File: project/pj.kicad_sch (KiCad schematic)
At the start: 2 parts, among them J1 RPi_GPIO

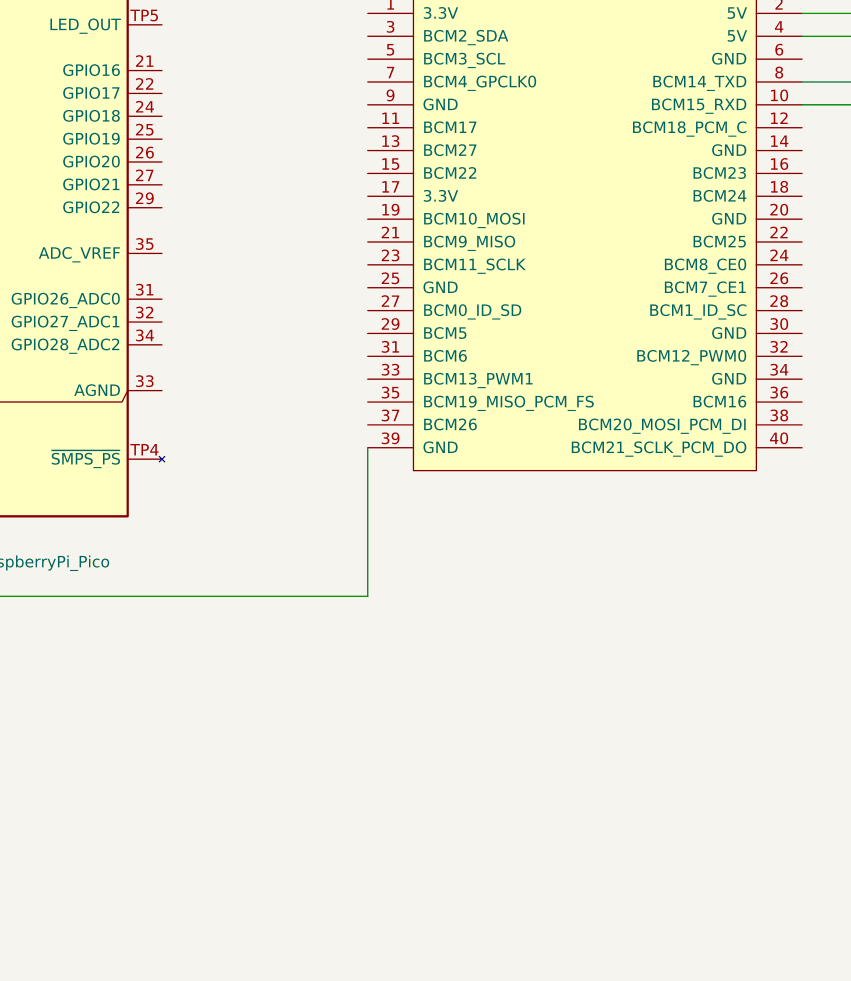
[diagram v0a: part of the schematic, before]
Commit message: all symbols linked to PCB
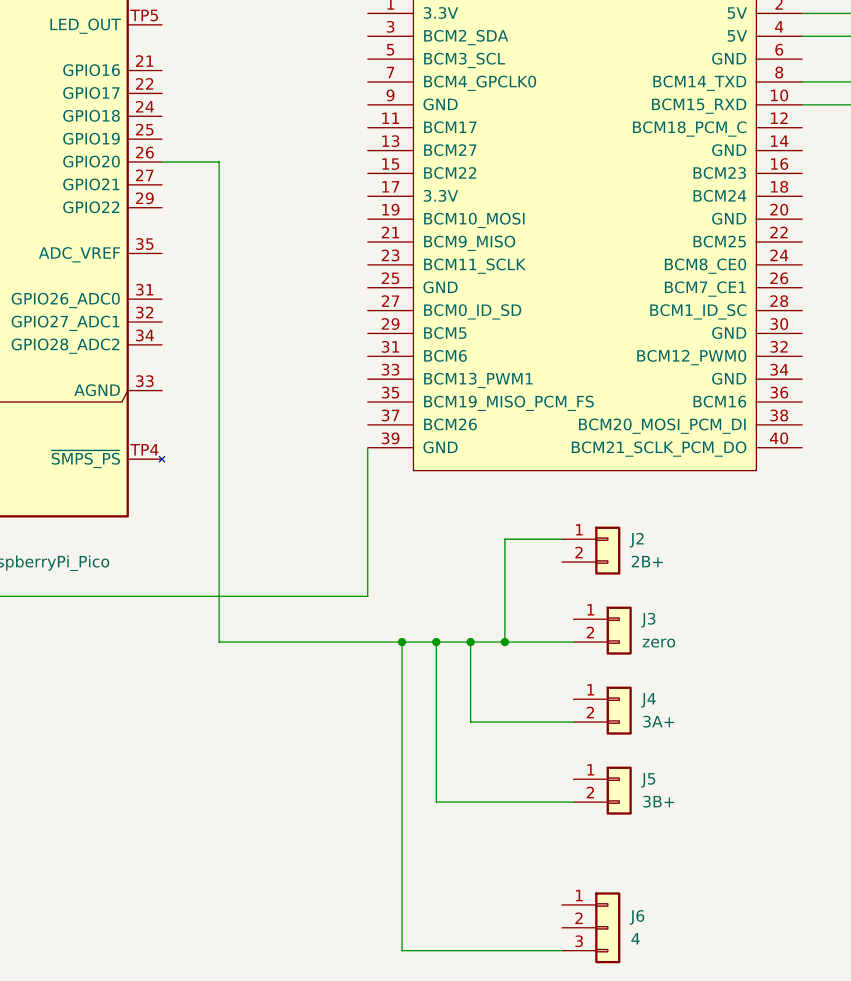
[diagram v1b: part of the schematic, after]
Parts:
- added J2: 2B+, Connector_PinHeader_2.54mm:PinHeader_1x02_P2.54mm_Vertical, symbol Connector_Generic:Conn_01x02
- added J3: zero, Connector_PinHeader_2.54mm:PinHeader_1x02_P2.54mm_Vertical, symbol Connector_Generic:Conn_01x02
- added J4: 3A+, Connector_PinHeader_2.54mm:PinHeader_1x02_P2.54mm_Vertical, symbol Connector_Generic:Conn_01x02
- added J5: 3B+, Connector_PinHeader_2.54mm:PinHeader_1x02_P2.54mm_Vertical, symbol Connector_Generic:Conn_01x02
- added J6: 4, Connector_PinHeader_2.54mm:PinHeader_1x03_P2.54mm_Vertical, symbol Connector_Generic:Conn_01x03
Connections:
- net at A1.26 (GPIO20): now also J2.1 (Pin_1), J3.2 (Pin_2), J4.2 (Pin_2), J5.2 (Pin_2), J6.3 (Pin_3)

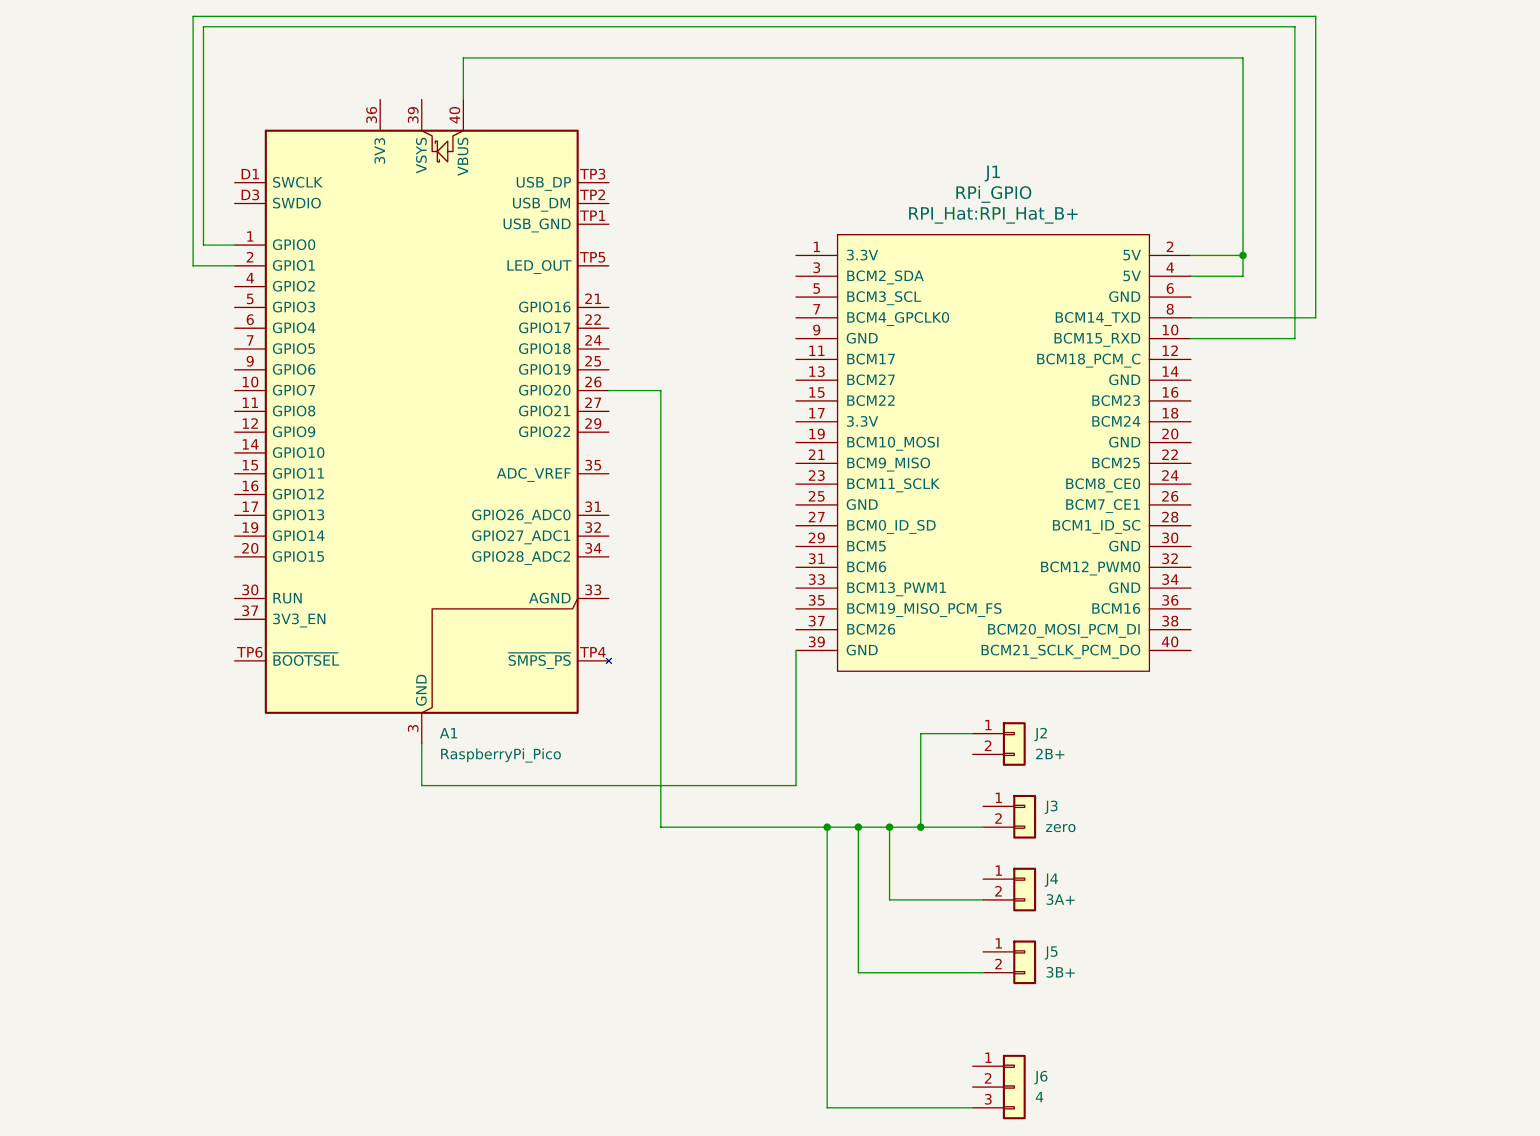
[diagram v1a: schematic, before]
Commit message: now with reset buttons
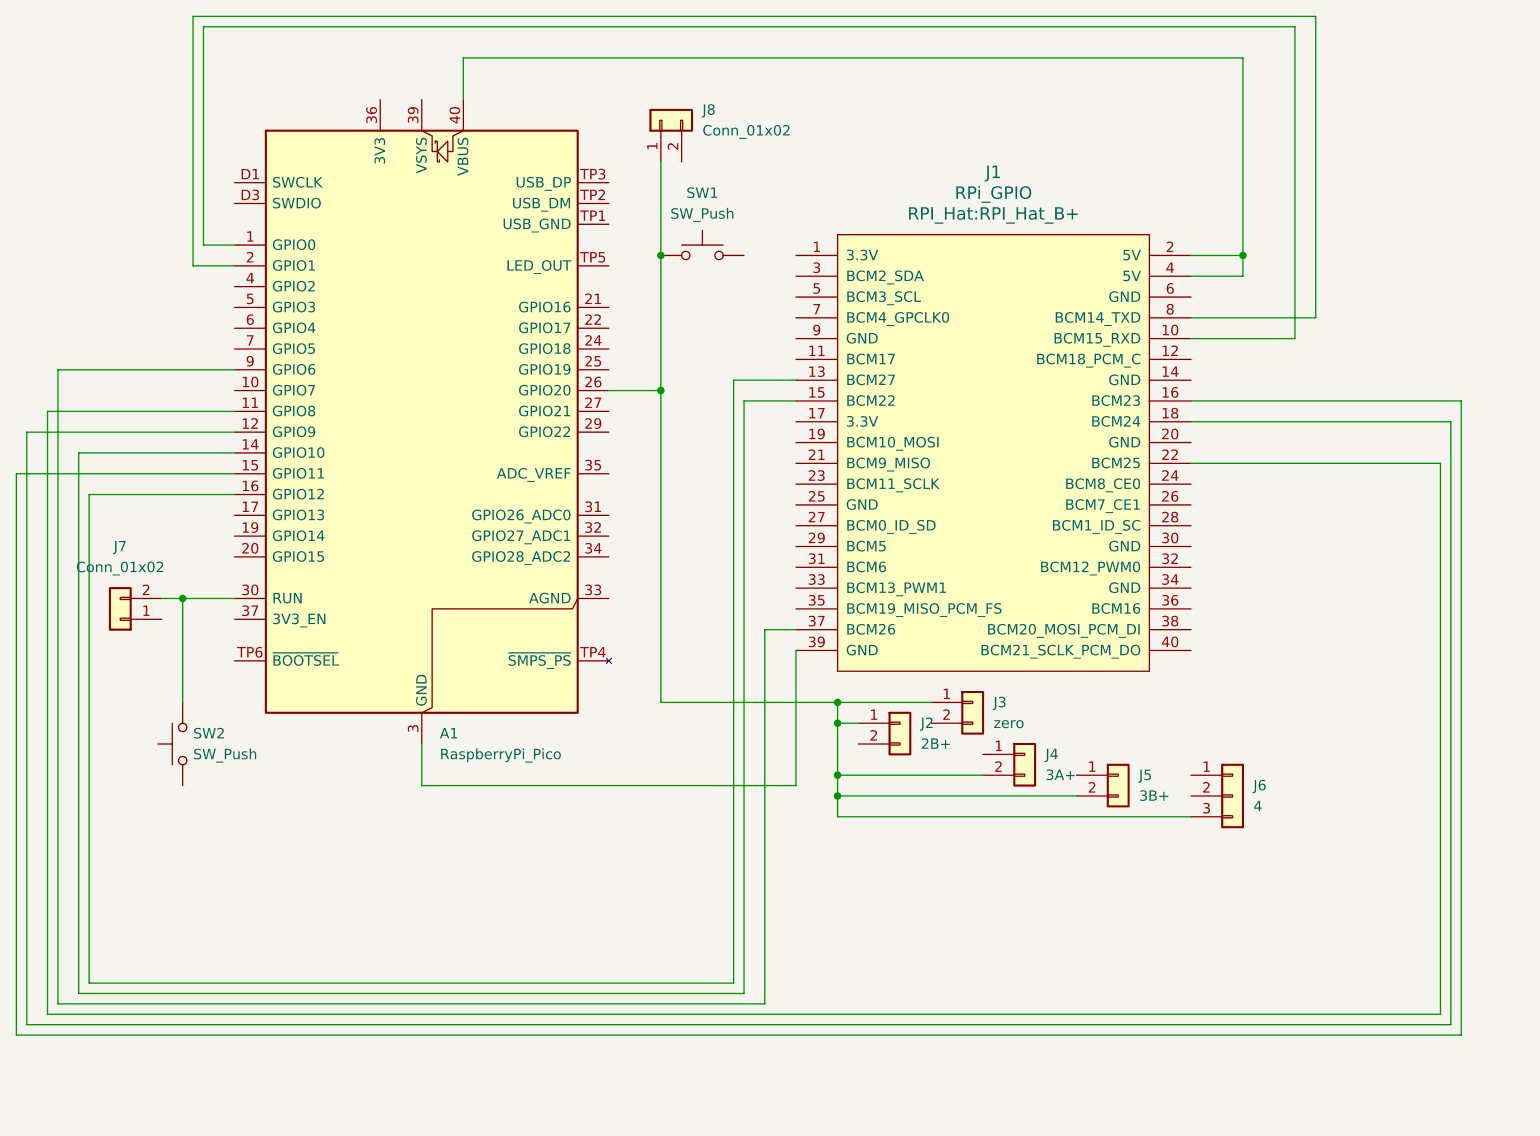
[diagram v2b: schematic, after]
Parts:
- added J7, J8: Conn_01x02, Connector_PinHeader_1.27mm:PinHeader_1x02_P1.27mm_Vertical, symbol Connector_Generic:Conn_01x02
- added SW1, SW2: SW_Push, Button_Switch_THT:SW_PUSH_6mm_H4.3mm, symbol Switch:SW_Push
- A1: footprint Module_RaspberryPi_Pico:RaspberryPi_Pico_Original_SMD -> Module_RaspberryPi_Pico:RaspberryPi_Pico_Common
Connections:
- net at A1.26 (GPIO20), J2.1 (Pin_1), J4.2 (Pin_2)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: now also J3.1 (Pin_1), J8.1 (Pin_1), SW1.1; no longer J3.2 (Pin_2)
- net at A1.11 (GPIO8): now also J1.22 (BCM25)
- net at A1.12 (GPIO9): now also J1.18 (BCM24)
- net at A1.14 (GPIO10): now also J1.15 (BCM22)
- net at A1.15 (GPIO11): now also J1.16 (BCM23)
- net at A1.16 (GPIO12): now also J1.13 (BCM27)
- net at A1.30 (RUN): now also J7.2 (Pin_2), SW2.2
- net at A1.9 (GPIO6): now also J1.37 (BCM26)
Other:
- moved on the sheet: J2, J3, J4, J5, J6

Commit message: now with grounds
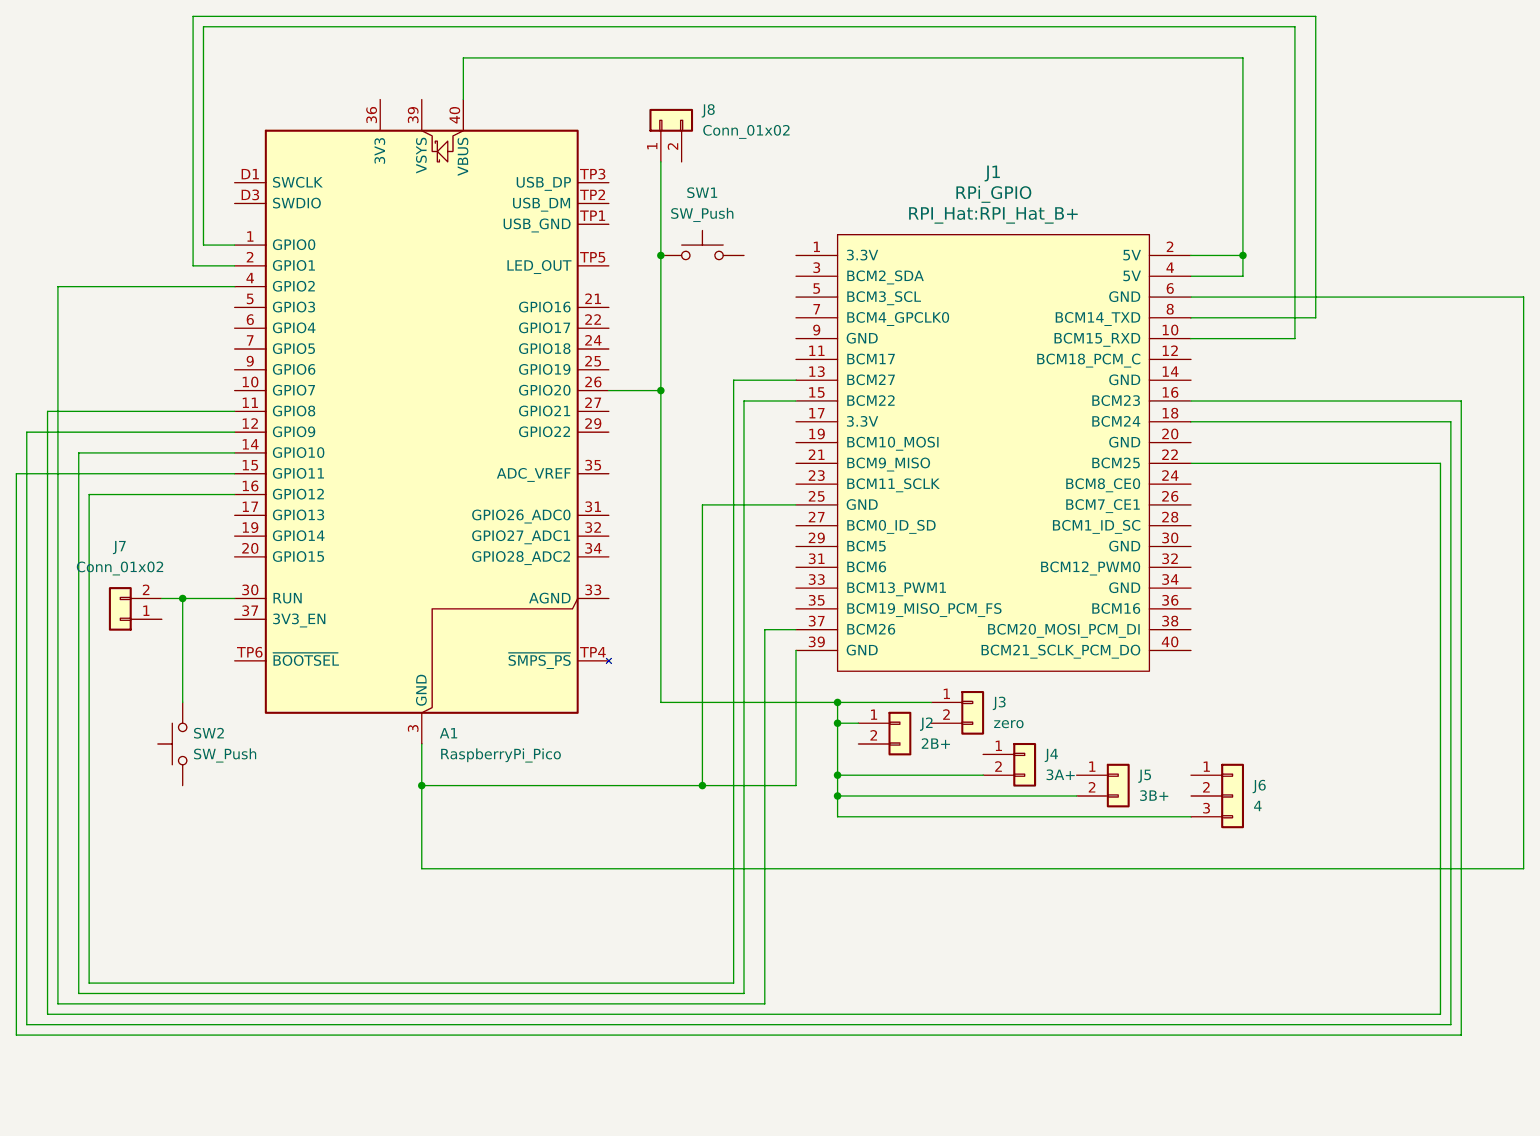
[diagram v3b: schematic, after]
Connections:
- net at A1.13 (GND), A1.18 (GND), A1.23 (GND)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: now also J1.25 (GND), J1.6 (GND)
- net at A1.4 (GPIO2): now also J1.37 (BCM26)
- net at A1.9 (GPIO6): no longer J1.37 (BCM26)
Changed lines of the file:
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@@
+	)
+	(junction
+		(at 86.36 120.65)
+		(diameter 0)
+		(color 0 0 0 0)
 	)
 	(junction
@@
 	)
 	(junction
+		(at 120.65 120.65)
+		(diameter 0)
+		(color 0 0 0 0)
+	)
+	(junction
 		(at 115.57 72.39)
 		(diameter 0)
@@
 	(wire
 		(pts
+			(xy 180.34 60.96) (xy 220.98 60.96)
+		)
+		(stroke
+			(width 0)
+			(type default)
+		)
+	)
+	(wire
+		(pts
 			(xy 195.58 63.5) (xy 195.58 26.67)
 		)
@@
 	(wire
 		(pts
+			(xy 220.98 130.81) (xy 86.36 130.81)
+		)
+		(stroke
+			(width 0)
+			(type default)
+		)
+	)
+	(wire
+		(pts
 			(xy 54.61 97.79) (xy 57.15 97.79)
 		)
@@
 	(wire
 		(pts
+			(xy 132.08 86.36) (xy 120.65 86.36)
+		)
+		(stroke
+			(width 0)
+			(type default)
+		)
+	)
+	(wire
+		(pts
 			(xy 128.27 101.6) (xy 128.27 147.32)
 		)
@@
 	(wire
 		(pts
+			(xy 120.65 120.65) (xy 86.36 120.65)
+		)
+		(stroke
+			(width 0)
+			(type default)
+		)
+	)
+	(wire
+		(pts
 			(xy 38.1 149.86) (xy 38.1 77.47)
 		)
@@
 	(wire
 		(pts
-			(xy 86.36 120.65) (xy 86.36 115.57)
-		)
-		(stroke
-			(width 0)
-			(type default)
-		)
-	)
-	(wire
-		(pts
 			(xy 45.72 85.09) (xy 45.72 144.78)
 		)
@@
 	(wire
 		(pts
-			(xy 63.5 69.85) (xy 41.91 69.85)
-		)
-		(stroke
-			(width 0)
-			(type default)
-		)
-	)
-	(wire
-		(pts
 			(xy 63.5 82.55) (xy 36.83 82.55)
 		)
@@
 	(wire
 		(pts
+			(xy 86.36 115.57) (xy 86.36 120.65)
+		)
+		(stroke
+			(width 0)
+			(type default)
+		)
+	)
+	(wire
+		(pts
 			(xy 63.5 85.09) (xy 45.72 85.09)
 		)
@@
 	(wire
 		(pts
-			(xy 132.08 120.65) (xy 86.36 120.65)
+			(xy 132.08 120.65) (xy 120.65 120.65)
 		)
 		(stroke
@@
 	(wire
 		(pts
+			(xy 120.65 86.36) (xy 120.65 120.65)
+		)
+		(stroke
+			(width 0)
+			(type default)
+		)
+	)
+	(wire
+		(pts
 			(xy 137.16 119.38) (xy 137.16 121.92)
 		)
@@
 	(wire
 		(pts
+			(xy 220.98 60.96) (xy 220.98 130.81)
+		)
+		(stroke
+			(width 0)
+			(type default)
+		)
+	)
+	(wire
+		(pts
 			(xy 195.58 26.67) (xy 58.42 26.67)
 		)
@@
 	(wire
 		(pts
-			(xy 41.91 69.85) (xy 41.91 147.32)
+			(xy 41.91 59.69) (xy 41.91 147.32)
+		)
+		(stroke
+			(width 0)
+			(type default)
+		)
+	)
+	(wire
+		(pts
+			(xy 86.36 120.65) (xy 86.36 130.81)
 		)
 		(stroke
@@
 		)
 		(stroke
+			(width 0)
+			(type default)
+		)
+	)
+	(wire
+		(pts
+			(xy 63.5 59.69) (xy 41.91 59.69)
+		)
+		(stroke

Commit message: RUN button GND
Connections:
- net GND: now reaches J8.2 (Pin_2)
- net GND: now also A1.13 (GND), A1.18 (GND), A1.23 (GND), A1.28 (GND), A1.3 (GND), A1.38 (GND), A1.8 (GND), A1.D2 (GND), J1.25 (GND), J1.39 (GND), J1.6 (GND), J7.1 (Pin_1), SW1.2, SW2.1
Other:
- moved on the sheet: SW1
